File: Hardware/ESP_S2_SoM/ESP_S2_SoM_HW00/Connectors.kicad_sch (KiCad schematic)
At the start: 4 parts, among them J1 DF40C-60DP-0.4V(51), J2 Bare PCB USB C

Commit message: ESP32 data is done
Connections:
- net IO39: now also J1.44; no longer J1.42
- net IO40: now also J1.46; no longer J1.44
- net IO41: now also J1.42; no longer J1.46
- net IO42: now also J1.52; no longer J1.48
- net RX0: now also J1.50; no longer J1.52
- net TX0: now also J1.48; no longer J1.50
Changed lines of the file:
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@@
     (effects (font (size 1.27 1.27)) (justify left bottom))
   )
-  (label "IO42" (at 175.26 114.3 0) (fields_autoplaced)
+  (label "IO42" (at 175.26 119.38 0) (fields_autoplaced)
     (effects (font (size 1.27 1.27)) (justify left bottom))
   )
@@
     (effects (font (size 1.27 1.27)) (justify left bottom))
   )
-  (label "IO40" (at 175.26 109.22 0) (fields_autoplaced)
+  (label "IO40" (at 175.26 111.76 0) (fields_autoplaced)
     (effects (font (size 1.27 1.27)) (justify left bottom))
   )
@@
     (effects (font (size 1.27 1.27)) (justify right bottom))
   )
-  (label "IO41" (at 175.26 111.76 0) (fields_autoplaced)
+  (label "IO41" (at 175.26 106.68 0) (fields_autoplaced)
     (effects (font (size 1.27 1.27)) (justify left bottom))
   )
-  (label "IO39" (at 175.26 106.68 0) (fields_autoplaced)
+  (label "IO39" (at 175.26 109.22 0) (fields_autoplaced)
     (effects (font (size 1.27 1.27)) (justify left bottom))
   )
@@
     (effects (font (size 1.27 1.27)) (justify left bottom))
   )
-  (label "RX0" (at 175.26 119.38 0) (fields_autoplaced)
+  (label "RX0" (at 175.26 116.84 0) (fields_autoplaced)
     (effects (font (size 1.27 1.27)) (justify left bottom))
   )
-  (label "TX0" (at 175.26 116.84 0) (fields_autoplaced)
+  (label "TX0" (at 175.26 114.3 0) (fields_autoplaced)
     (effects (font (size 1.27 1.27)) (justify left bottom))
   )

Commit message: working on power routing
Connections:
- net +3V3: now also J1.18, J1.20
- net GND: now also J1.22, J1.24
- net RX0: now also J1.48; no longer J1.50
- net TX0: now also J1.50; no longer J1.48
- net VBAT: now also J1.4, J1.6, J1.8
- net VBUS: now also J1.10, J1.12
- net VSYS: now also J1.14, J1.16

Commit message: Routing is done
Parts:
- added C415: 100n, Capacitor_SMD:C_0201_0603Metric, symbol Component lib:C
- added R103: 220k, Resistor_SMD:R_0201_0603Metric, symbol Component_lib:R
- added R104: 470k, Resistor_SMD:R_0201_0603Metric, symbol Component_lib:R
- renumbered J1 to J101, J2 to J102
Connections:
- net BATTERY_TEMP: now also J101.3
- net GND: now also C415.2, R104.2
- net IO1: now also C415.1, R103.2, R104.1; no longer J101.3
- net VBAT: now also R103.1
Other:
- note added: "6uA leakage"

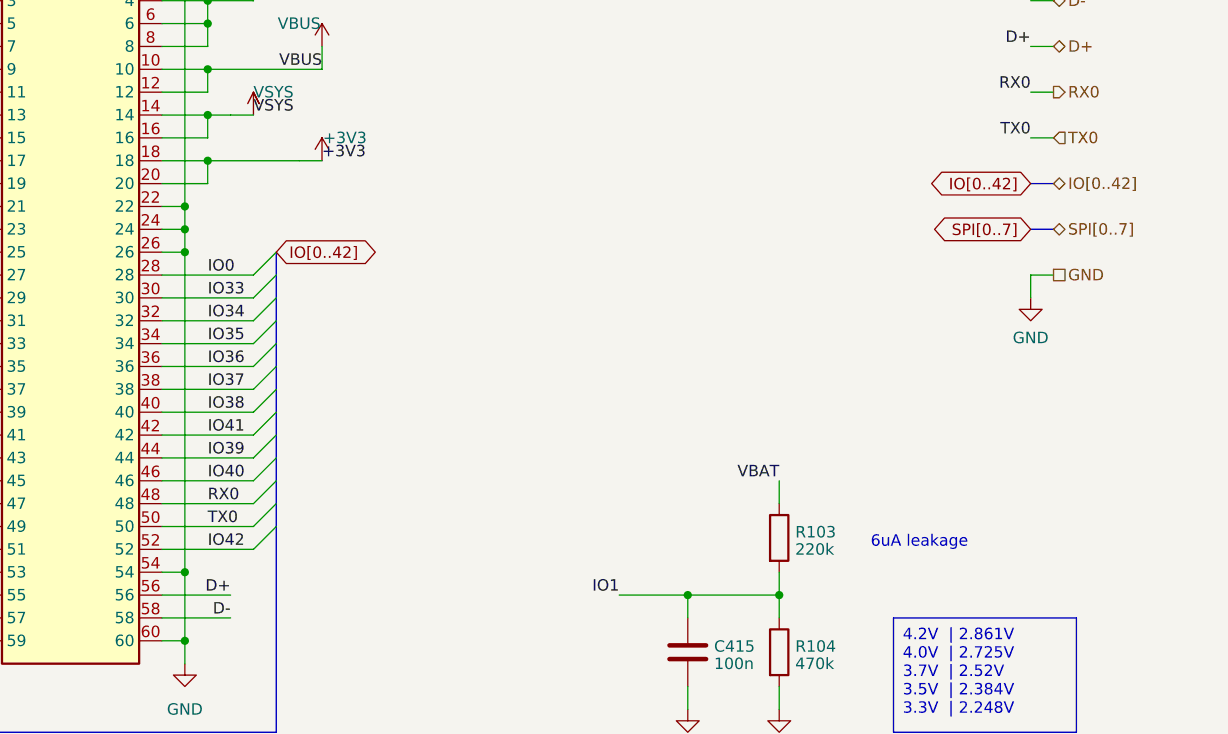
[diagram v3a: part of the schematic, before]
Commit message: quick pinout adjustement
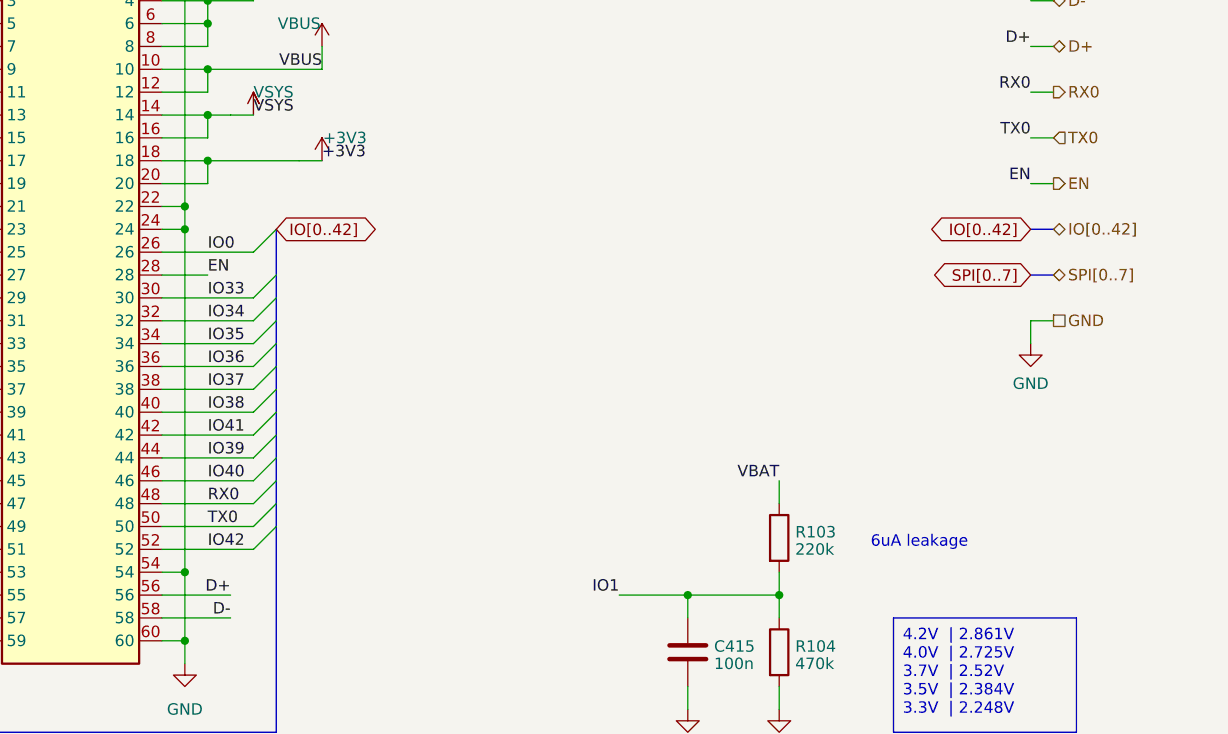
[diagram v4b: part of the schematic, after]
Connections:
- net GND: no longer J101.26
- net IO0: now also J101.26; no longer J101.28
- new net EN: J101.28
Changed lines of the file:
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@@
   (junction (at 66.04 63.5) (diameter 0) (color 0 0 0 0)
-  )
-  (junction (at 172.72 86.36) (diameter 0) (color 0 0 0 0)
   )
   (no_connect (at 63.5 81.28))
@@
     (stroke (width 0) (type default))
   )
-  (bus_entry (at 180.34 88.9) (size 2.54 -2.54)
+  (bus_entry (at 180.34 86.36) (size 2.54 -2.54)
     (stroke (width 0) (type default))
   )
@@
     (stroke (width 0) (type default))
   )
-  (wire (pts (xy 170.18 86.36) (xy 172.72 86.36))
-    (stroke (width 0) (type default))
-  )
   (wire (pts (xy 170.18 76.2) (xy 175.26 76.2))
     (stroke (width 0) (type default))
@@
     (stroke (width 0) (type default))
   )
-  (wire (pts (xy 172.72 83.82) (xy 172.72 86.36))
-    (stroke (width 0) (type default))
-  )
   (bus (pts (xy 137.16 101.6) (xy 137.16 104.14))
     (stroke (width 0) (type default))
@@
     (stroke (width 0) (type default))
   )
-  (bus (pts (xy 266.7 83.82) (xy 269.24 83.82))
+  (bus (pts (xy 266.7 88.9) (xy 269.24 88.9))
     (stroke (width 0) (type default))
   )
@@
     (stroke (width 0) (type default))
   )
-  (wire (pts (xy 172.72 86.36) (xy 172.72 121.92))
+  (wire (pts (xy 172.72 83.82) (xy 172.72 121.92))
     (stroke (width 0) (type default))
   )
@@
   )
   (wire (pts (xy 175.26 66.04) (xy 187.96 66.04))
+    (stroke (width 0) (type default))
+  )
+  (wire (pts (xy 170.18 88.9) (xy 175.26 88.9))
     (stroke (width 0) (type default))
   )
@@
     (stroke (width 0.3) (type default) (color 0 0 0 1))
   )
-  (wire (pts (xy 266.7 91.44) (xy 266.7 88.9))
+  (wire (pts (xy 266.7 96.52) (xy 266.7 93.98))
     (stroke (width 0.3) (type default) (color 0 0 0 1))
   )
@@
     (stroke (width 0) (type default))
   )
-  (bus (pts (xy 182.88 86.36) (xy 182.88 88.9))
-    (stroke (width 0) (type default))
-  )
-  (wire (pts (xy 170.18 88.9) (xy 180.34 88.9))
+  (bus (pts (xy 182.88 83.82) (xy 182.88 88.9))
+    (stroke (width 0) (type default))
+  )
+  (wire (pts (xy 266.7 78.74) (xy 269.24 78.74))
     (stroke (width 0) (type default))
   )
@@
     (stroke (width 0) (type default))
   )
-  (bus (pts (xy 266.7 78.74) (xy 269.24 78.74))
+  (wire (pts (xy 170.18 86.36) (xy 180.34 86.36))
+    (stroke (width 0) (type default))
+  )
+  (bus (pts (xy 266.7 83.82) (xy 269.24 83.82))
     (stroke (width 0) (type default))
   )
@@
     (stroke (width 0) (type default))
   )
-  (wire (pts (xy 266.7 88.9) (xy 269.24 88.9))
+  (wire (pts (xy 266.7 93.98) (xy 269.24 93.98))
     (stroke (width 0.3) (type default) (color 0 0 0 1))
   )
@@
     (effects (font (size 1.27 1.27)) (justify left bottom))
   )
+  (label "EN" (at 266.7 78.74 180) (fields_autoplaced)
+    (effects (font (size 1.27 1.27)) (justify right bottom))
+  )
   (label "TX0" (at 266.7 73.66 180) (fields_autoplaced)
     (effects (font (size 1.27 1.27)) (justify right bottom))
@@
     (effects (font (size 1.27 1.27)) (justify left bottom))
   )
-  (label "IO0" (at 175.26 88.9 0) (fields_autoplaced)
+  (label "IO0" (at 175.26 86.36 0) (fields_autoplaced)
+    (effects (font (size 1.27 1.27)) (justify left bottom))
+  )
+  (label "EN" (at 175.26 88.9 0) (fields_autoplaced)
     (effects (font (size 1.27 1.27)) (justify left bottom))
   )
@@
     (effects (font (size 1.27 1.27)) (justify left bottom))
   )
-  (global_label "IO[0..42]" (shape bidirectional) (at 182.88 86.36 0) (fields_autoplaced)
+  (global_label "IO[0..42]" (shape bidirectional) (at 182.88 83.82 0) (fields_autoplaced)
     (effects (font (size 1.27 1.27)) (justify left))
-    (property "Intersheetrefs" "${INTERSHEET_REFS}" (at 195.3639 86.36 0)
+    (property "Intersheetrefs" "${INTERSHEET_REFS}" (at 195.3639 83.82 0)
       (effects (font (size 1.27 1.27)) (justify left) hide)
     )
@@
     )
   )
-  (global_label "IO[0..42]" (shape bidirectional) (at 266.7 78.74 180) (fields_autoplaced)
+  (global_label "IO[0..42]" (shape bidirectional) (at 266.7 83.82 180) (fields_autoplaced)
     (effects (font (size 1.27 1.27)) (justify right))
-    (property "Intersheetrefs" "${INTERSHEET_REFS}" (at 254.2161 78.74 0)
+    (property "Intersheetrefs" "${INTERSHEET_REFS}" (at 254.2161 83.82 0)
       (effects (font (size 1.27 1.27)) (justify right) hide)
     )
   )
-  (global_label "SPI[0..7]" (shape bidirectional) (at 266.7 83.82 180) (fields_autoplaced)
+  (global_label "SPI[0..7]" (shape bidirectional) (at 266.7 88.9 180) (fields_autoplaced)
     (effects (font (size 1.27 1.27)) (justify right))
-    (property "Intersheetrefs" "${INTERSHEET_REFS}" (at 254.2766 83.82 0)
+    (property "Intersheetrefs" "${INTERSHEET_REFS}" (at 254.2766 88.9 0)
       (effects (font (size 1.27 1.27)) (justify right) hide)
     )
@@
     (effects (font (size 1.27 1.27)) (justify left))
   )
+  (hierarchical_label "EN" (shape output) (at 269.24 78.74 0) (fields_autoplaced)
+    (effects (font (size 1.27 1.27)) (justify left))
+  )
   (hierarchical_label "+3V3" (shape input) (at 269.24 40.64 0) (fields_autoplaced)
     (effects (font (size 1.27 1.27)) (justify left))
@@
     (effects (font (size 1.27 1.27)) (justify left))
   )
-  (hierarchical_label "GND" (shape passive) (at 269.24 88.9 0) (fields_autoplaced)
+  (hierarchical_label "GND" (shape passive) (at 269.24 93.98 0) (fields_autoplaced)
     (effects (font (size 1.27 1.27)) (justify left))
   )
-  (hierarchical_label "SPI[0..7]" (shape bidirectional) (at 269.24 83.82 0) (fields_autoplaced)
+  (hierarchical_label "SPI[0..7]" (shape bidirectional) (at 269.24 88.9 0) (fields_autoplaced)
     (effects (font (size 1.27 1.27)) (justify left))
   )
-  (hierarchical_label "IO[0..42]" (shape bidirectional) (at 269.24 78.74 0) (fields_autoplaced)
+  (hierarchical_label "IO[0..42]" (shape bidirectional) (at 269.24 83.82 0) (fields_autoplaced)
     (effects (font (size 1.27 1.27)) (justify left))
   )
@@
     )
   )
-  (symbol (lib_id "power:GND") (at 266.7 91.44 0) (unit 1)
+  (symbol (lib_id "power:GND") (at 266.7 96.52 0) (unit 1)
     (in_bom yes) (on_board yes) (dnp no) (fields_autoplaced)
-    (property "Reference" "#PWR0118" (at 266.7 97.79 0)
-      (effects (font (size 1.27 1.27)) hide)
-    )
-    (property "Value" "GND" (at 266.7 95.8834 0)
+    (property "Reference" "#PWR0118" (at 266.7 102.87 0)
+      (effects (font (size 1.27 1.27)) hide)
+    )
+    (property "Value" "GND" (at 266.7 100.9634 0)
       (effects (font (size 1.27 1.27)))
     )
-    (property "Footprint" "" (at 266.7 91.44 0)
-      (effects (font (size 1.27 1.27)) hide)
-    )
-    (property "Datasheet" "" (at 266.7 91.44 0)
-      (effects (font (size 1.27 1.27)) hide)
-    )
+    (property "Footprint" "" (at 266.7 96.52 0)
+      (effects (font (size 1.27 1.27)) hide)
+    )
+    (property "Datasheet" "" (at 266.7 96.52 0)
+      (effects (font (size 1.27 1.27)) hide)
+    )

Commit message: Small cartouche mistake
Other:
- title: PSoM - ESP S3 -> PSoM - ESP S2
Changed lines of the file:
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@@
   (paper "A4")
   (title_block
-    (title "PSoM - ESP S3")
+    (title "PSoM - ESP S2")
     (date "2023-04-17")
     (rev "HW00")
